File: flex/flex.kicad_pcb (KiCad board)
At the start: 2 copper layers, 104.1 x 90.6 mm, 73 parts, among them J1 NA_Conn_01x04_Female, J2 NA_Conn_01x05_Female, J3 NA_Conn_01x03_Female, J4 NA_Conn_01x06_Female, J5 NA_Conn_01x03_Female, SW10 NA_SW_Push, SW11 NA_SW_Push, SW12 NA_SW_Push, SW15 NA_SW_Push, SW16 NA_SW_Push, SW17 NA_SW_Push, SW20 NA_SW_Push, SW21 NA_SW_Push, SW22 NA_SW_Push, SW24 NA_SW_Push, SW25 NA_SW_Push, SW26 NA_SW_Push, SW6 NA_SW_Push, SW7 NA_SW_Push, SW8 NA_SW_Push

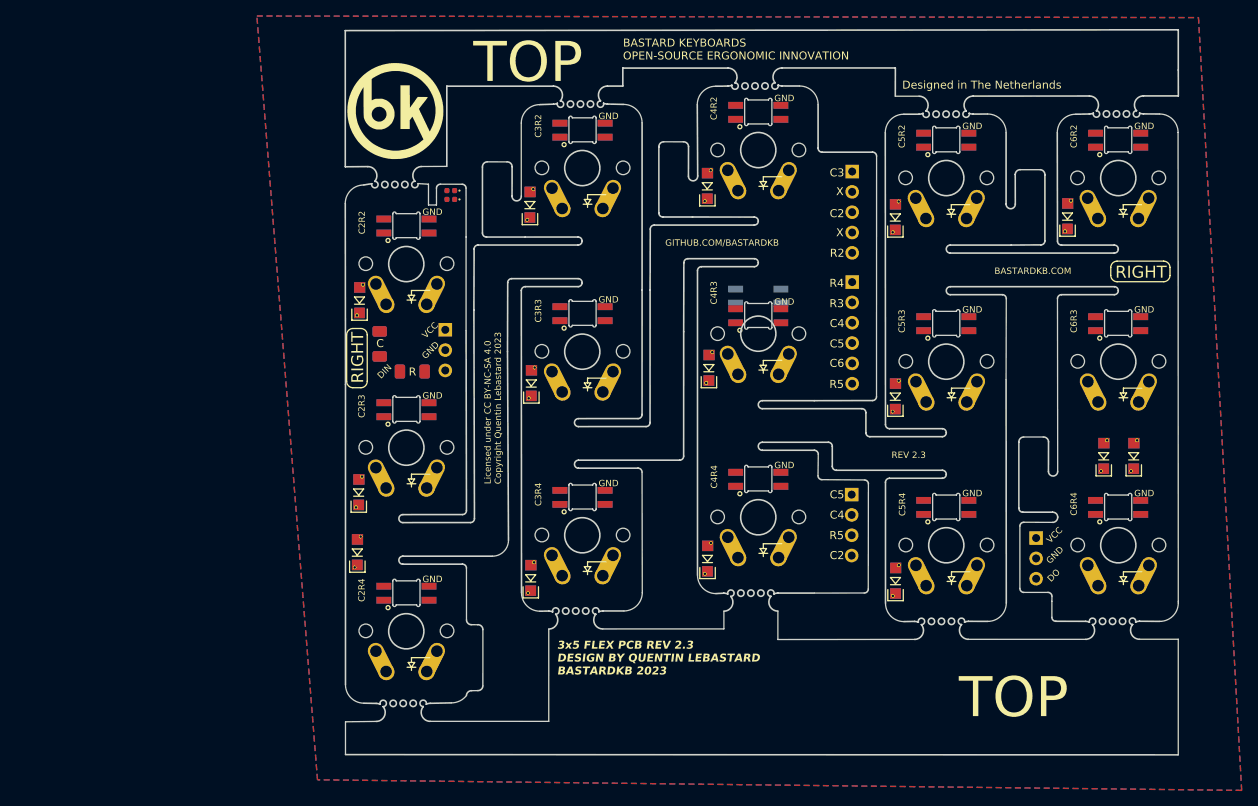
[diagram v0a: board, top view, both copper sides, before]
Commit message: update diode footprints
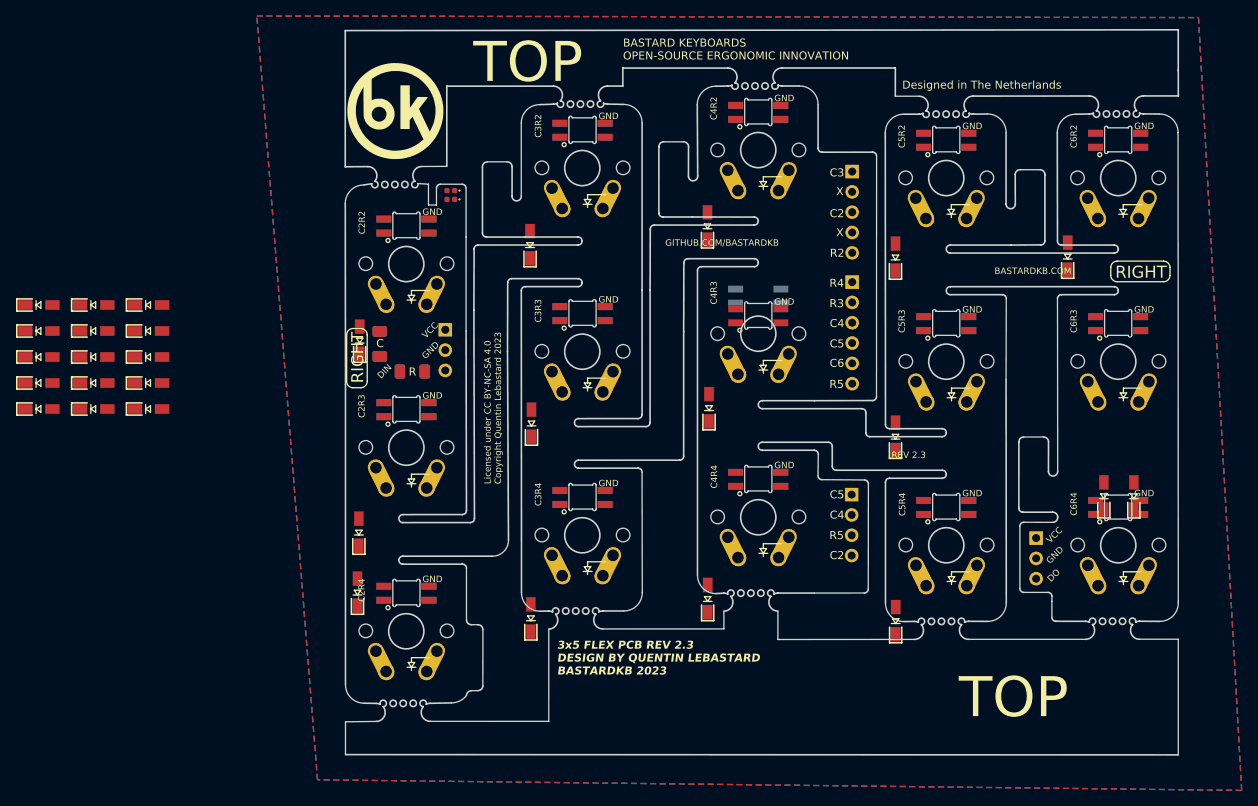
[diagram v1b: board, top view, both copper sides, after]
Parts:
- added D10: LEFT_D, customs:SOD123_assembly, F.Cu at (19.3, 83.4)
- added D18: LEFT_D, customs:SOD123_assembly, F.Cu at (19.3, 86.7)
- added D28: LEFT_D, customs:SOD123_assembly, F.Cu at (19.3, 89.9)
- added D29: LEFT_D, customs:SOD123_assembly, F.Cu at (19.3, 93.2)
- added D30: LEFT_D, customs:SOD123_assembly, F.Cu at (19.3, 96.4)
- added D43: LEFT_D, customs:SOD123_assembly, F.Cu at (26.1, 83.4)
- added D44: LEFT_D, customs:SOD123_assembly, F.Cu at (26.1, 86.7)
- added D45: LEFT_D, customs:SOD123_assembly, F.Cu at (26.1, 89.9)
- added D46: LEFT_D, customs:SOD123_assembly, F.Cu at (26.1, 93.2)
- added D53: LEFT_D, customs:SOD123_assembly, F.Cu at (26.1, 96.4)
- added D54: LEFT_D, customs:SOD123_assembly, F.Cu at (33.0, 83.4)
- added D61: LEFT_D, customs:SOD123_assembly, F.Cu at (33.0, 86.7)
- added D62: LEFT_D, customs:SOD123_assembly, F.Cu at (33.0, 89.9)
- added D63: LEFT_D, customs:SOD123_assembly, F.Cu at (33.0, 93.2)
- added D64: LEFT_D, customs:SOD123_assembly, F.Cu at (33.0, 96.4)
- D11, D12, D13, D14, D15, D16, D17, D19, D20, D27, D31, D32, D35, D36, D9: value NA_D -> RIGHT_D; footprint custom:Diode_TH_SOD123 -> customs:SOD123_assembly
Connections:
- SW12 pad 1: Net-(SW12-Pad1) -> row4
- SW17 pad 1: Net-(SW12-Pad1) -> row4
- SW21 pad 1: unconnected-(SW21-Pad1) -> row3
- SW22 pad 1: unconnected-(SW22-Pad1) -> row4
- SW25 pad 1: unconnected-(SW25-Pad1) -> row3
- SW26 pad 1: unconnected-(SW26-Pad1) -> row4

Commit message: place diodes
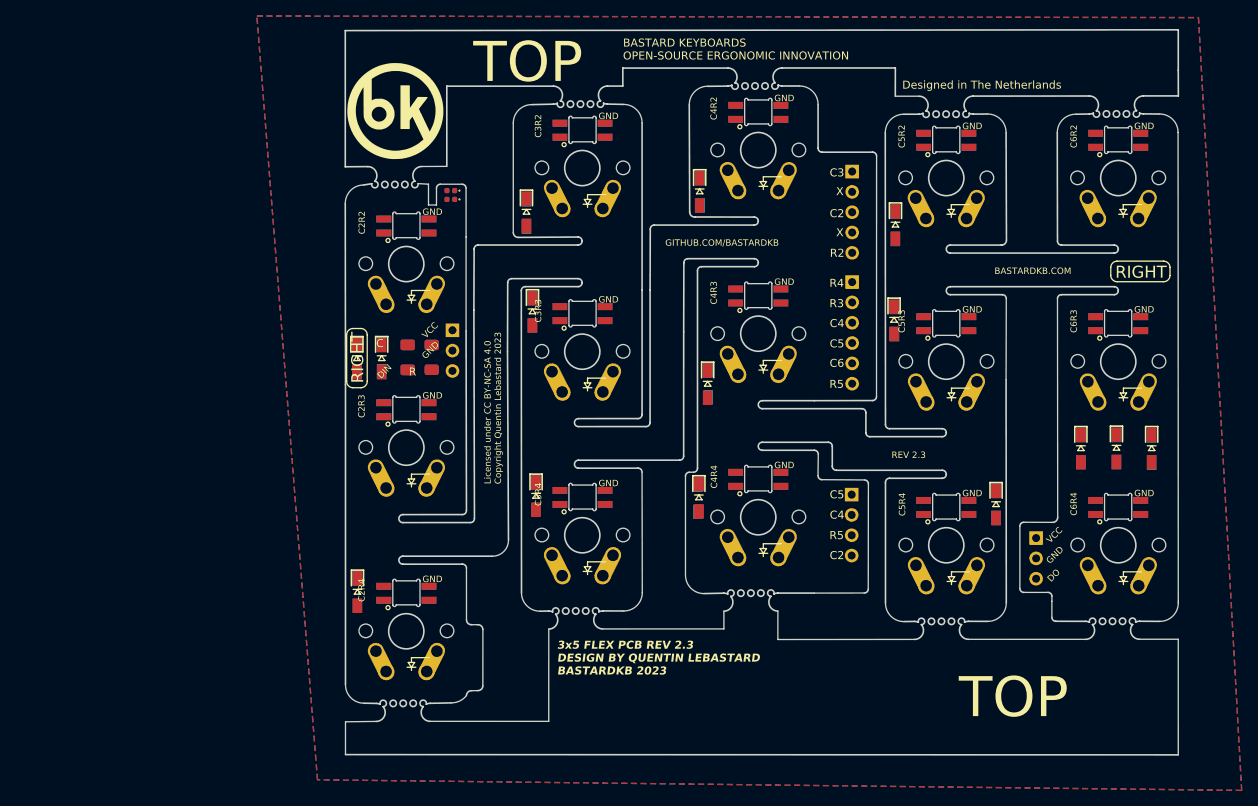
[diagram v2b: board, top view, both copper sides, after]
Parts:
- D10, D18, D28, D29, D30, D43, D44, D45, D46, D53, D54, D61, D62, D63, D64: moved to B.Cu
- moved D64 125.5 mm to (158.4, 101.4), turned to -90 degrees
- moved D63 121.3 mm to (154.0, 101.3), turned to -90 degrees
- moved D62 117.1 mm to (149.6, 101.3), turned to -90 degrees
- moved D53 113.4 mm to (138.9, 108.3), turned to -90 degrees
- moved D61 94.3 mm to (126.3, 73.5), turned to -90 degrees
- moved D54 93.3 mm to (126.2, 85.3), turned to -90 degrees
- moved D44 77.8 mm to (102.0, 69.2), turned to -90 degrees
- moved D46 76.9 mm to (101.7, 107.5), turned to -90 degrees
- moved D45 76.9 mm to (103.0, 93.2), turned to -90 degrees
- moved D30 62.9 mm to (81.0, 84.2), turned to -90 degrees
- moved D18 62.7 mm to (80.2, 71.9), turned to -90 degrees
- moved D43 60.2 mm to (81.5, 107.3), turned to -90 degrees
- moved D29 47.6 mm to (59.1, 119.3), turned to -90 degrees
- moved D28 42.9 mm to (62.1, 90.0), turned to -90 degrees
- moved D10 40.3 mm to (59.0, 90.1), turned to -90 degrees
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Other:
- outline, holes or cut-outs redrawn

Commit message: add mouse bite footprints
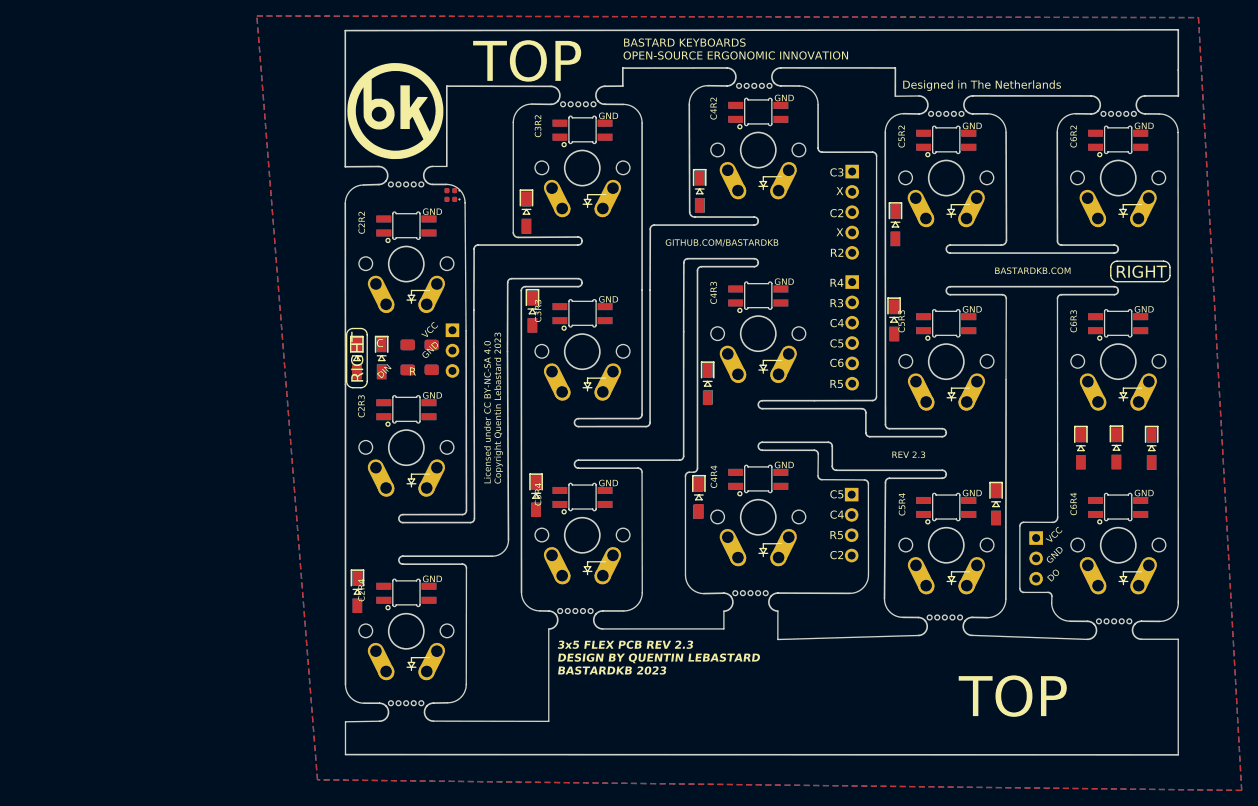
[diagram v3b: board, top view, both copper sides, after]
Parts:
- added Mousebite1: ~, customs:mousebite, F.Cu at (65.2, 68.3)
- added Mousebite10: ~, customs:mousebite, F.Cu at (153.7, 122.9)
- added Mousebite2: ~, customs:mousebite, F.Cu at (86.7, 58.3)
- added Mousebite3: ~, customs:mousebite, F.Cu at (108.7, 56.0)
- added Mousebite4: ~, customs:mousebite, F.Cu at (132.7, 59.5)
- added Mousebite5: ~, customs:mousebite, F.Cu at (154.3, 59.5)
- added Mousebite6: ~, customs:mousebite, F.Cu at (65.2, 133.2)
- added Mousebite7: ~, customs:mousebite, F.Cu at (86.4, 121.7)
- added Mousebite8: ~, customs:mousebite, F.Cu at (108.3, 119.4)
- added Mousebite9: ~, customs:mousebite, F.Cu at (132.5, 122.5)
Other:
- outline, holes or cut-outs redrawn
